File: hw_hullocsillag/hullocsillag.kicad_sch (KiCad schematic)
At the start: 38 parts, among them J1 Conn_2Rows-05Pins, Q1 AO3401A, Q2 AO3401A, Q3 AO3401A, SW2 SW_DPST_x2, T1 Tab, T2 Tab, T3 Tab, U1 PY32F002AF15P6TU

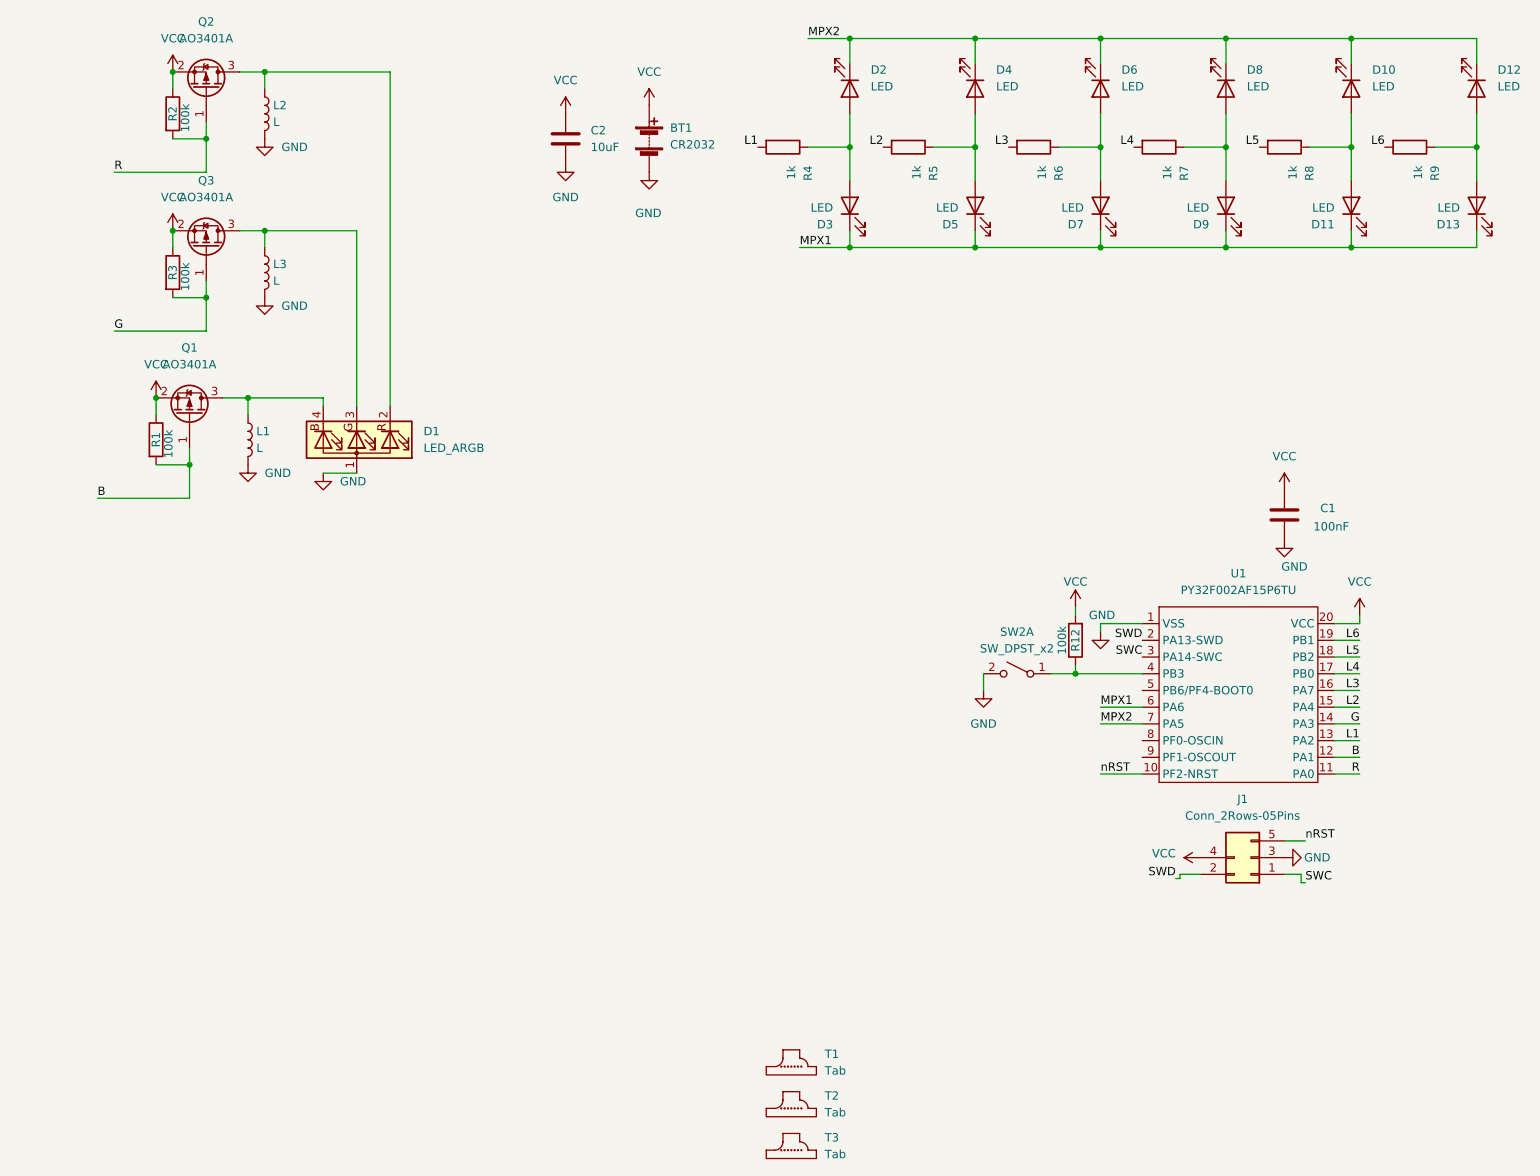
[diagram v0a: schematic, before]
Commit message: Hullocsillag updated, new led driver
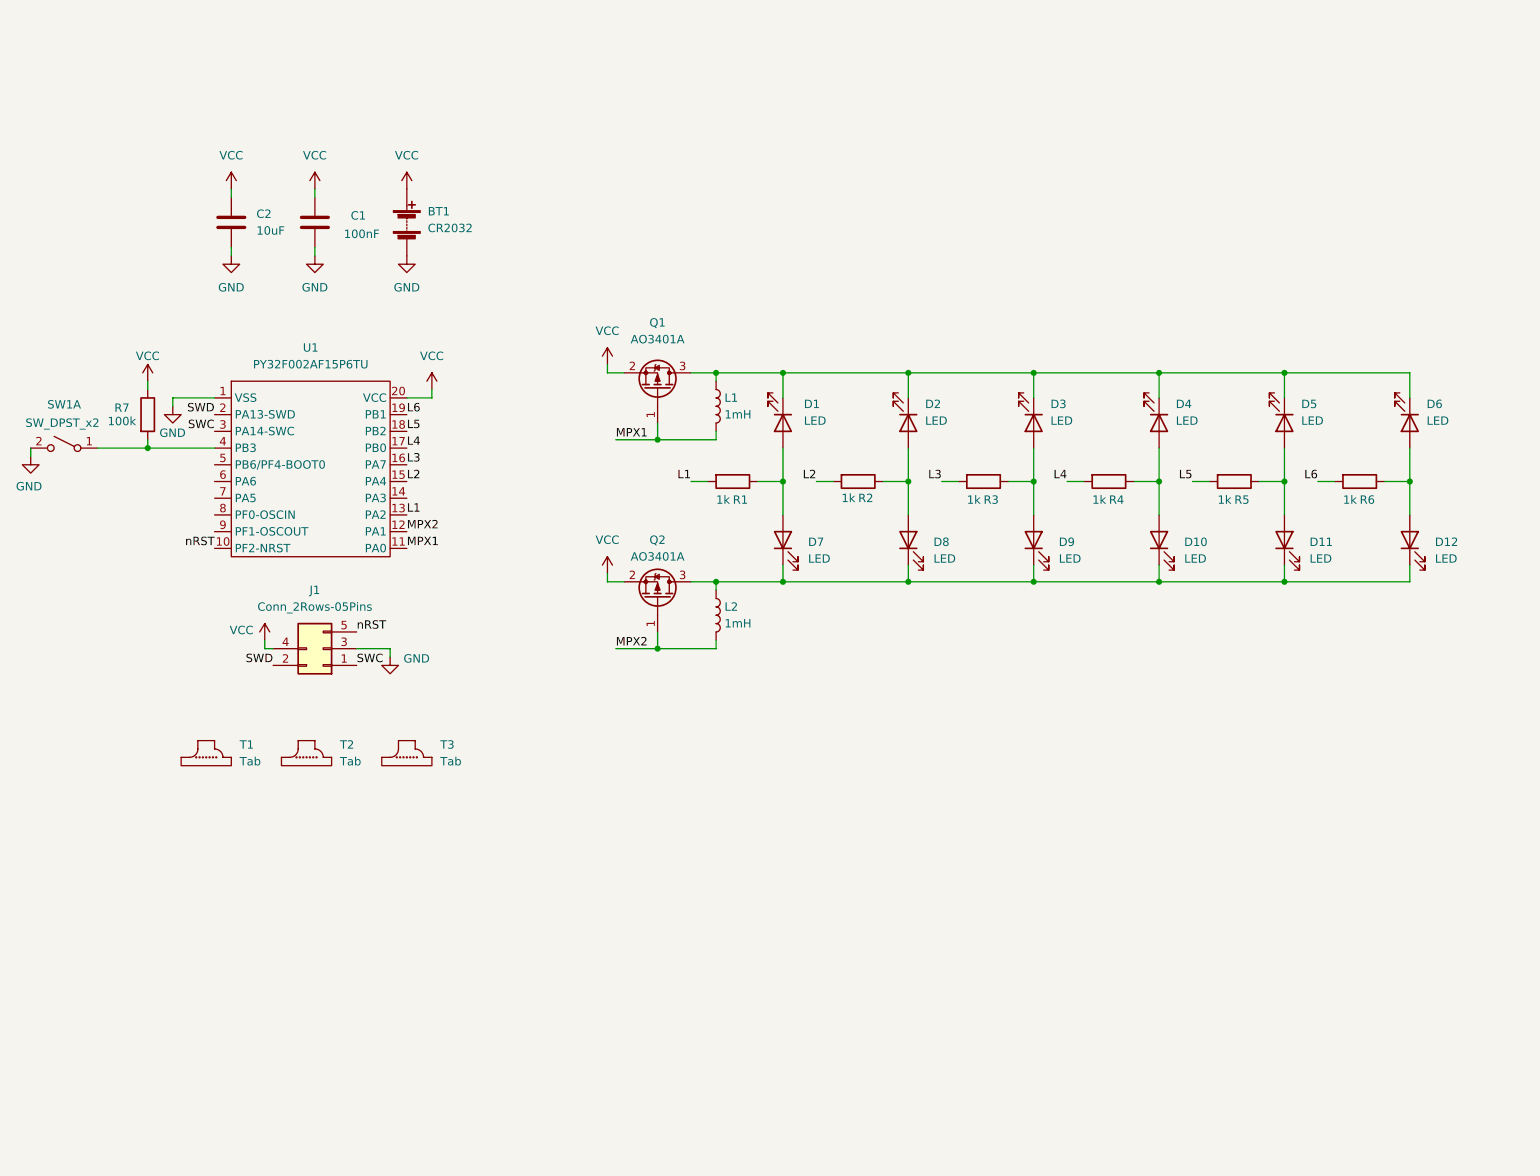
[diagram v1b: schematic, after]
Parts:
- removed D1: LED_ARGB, hullocsillag:LED_RGB_Wuerth-PLCC4_3.2x2.8mm_150141M173100, symbol Device:LED_ARGB
- removed L3: L, Inductor_SMD:L_1008_2520Metric, symbol Device:L
- removed Q3: AO3401A, hullocsillag:SOT-23, symbol Transistor_FET:AO3401A
- removed R1, R12, R2, R3: 100k, Resistor_SMD:R_0603_1608Metric, symbol Device:R
- added R7: 100k, Resistor_SMD:R_0603_1608Metric, symbol Device:R
- L1, L2: value L -> 1mH
- renumbered D2 to D1, D9 to D10, D13 to D12, D4 to D2, D6 to D3, D8 to D4, D10 to D5, D12 to D6, D3 to D7, D5 to D8, D7 to D9, R4 to R1, R5 to R2, R6 to R3, R7 to R4, R8 to R5, R9 to R6, SW2 to SW1
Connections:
- net GND: no longer L1.2, L2.2
- net MPX1: now also L1.2, Q1.1 (G), U1.11 (PA0); no longer D10.1 (K), D11.1 (K), D12.1 (K), D7.1 (K), D8.1 (K), D9.1 (K), U1.6 (PA6)
- net MPX2: now also L2.2, Q2.1 (G), U1.12 (PA1); no longer D1.1 (K), D2.1 (K), D3.1 (K), D4.1 (K), D5.1 (K), D6.1 (K), U1.7 (PA5)
- net VCC: now also R7.1
- net at SW1.1 (A), U1.4 (PB3): now also R7.2
- net at L2.1, Q2.3 (D): now also D10.1 (K), D11.1 (K), D12.1 (K), D7.1 (K), D8.1 (K), D9.1 (K)
- net at L1.1, Q1.3 (D): now also D1.1 (K), D2.1 (K), D3.1 (K), D4.1 (K), D5.1 (K), D6.1 (K)
- removed net B: Q1.1 (G), U1.12 (PA1)
- net G: no longer names the net of U1.14 (PA3)
- removed net R: Q2.1 (G), U1.11 (PA0)
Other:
- moved on the sheet: BT1, C1, C2, D1, D10, D11, D12, D2, D3, D4, D5, D6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

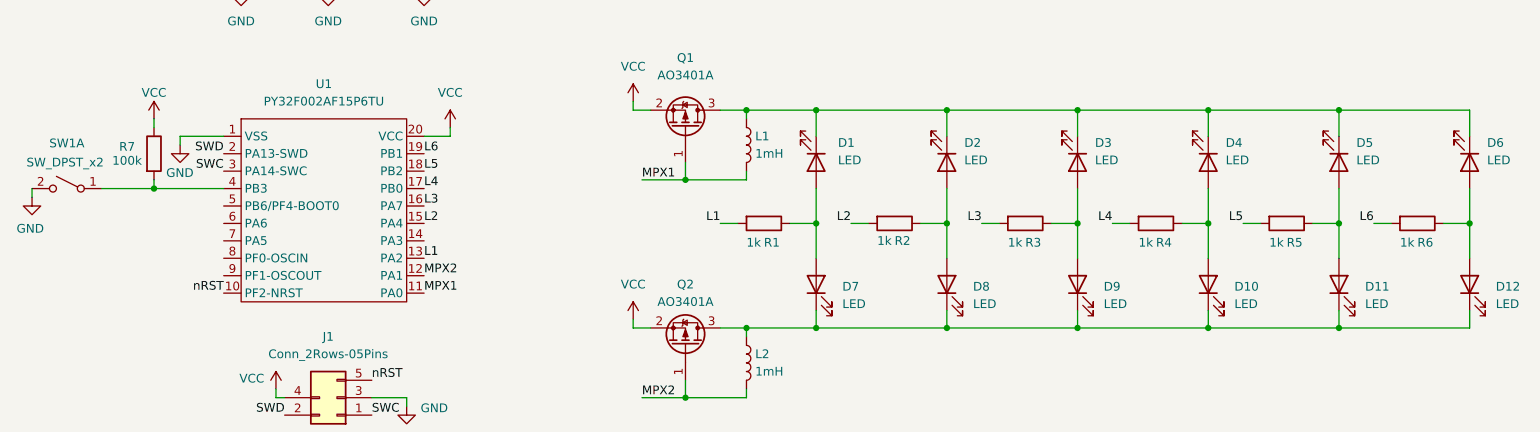
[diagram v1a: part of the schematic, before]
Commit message: Hullocsillag routed, C2 capacitor relocated, silkscreen added.
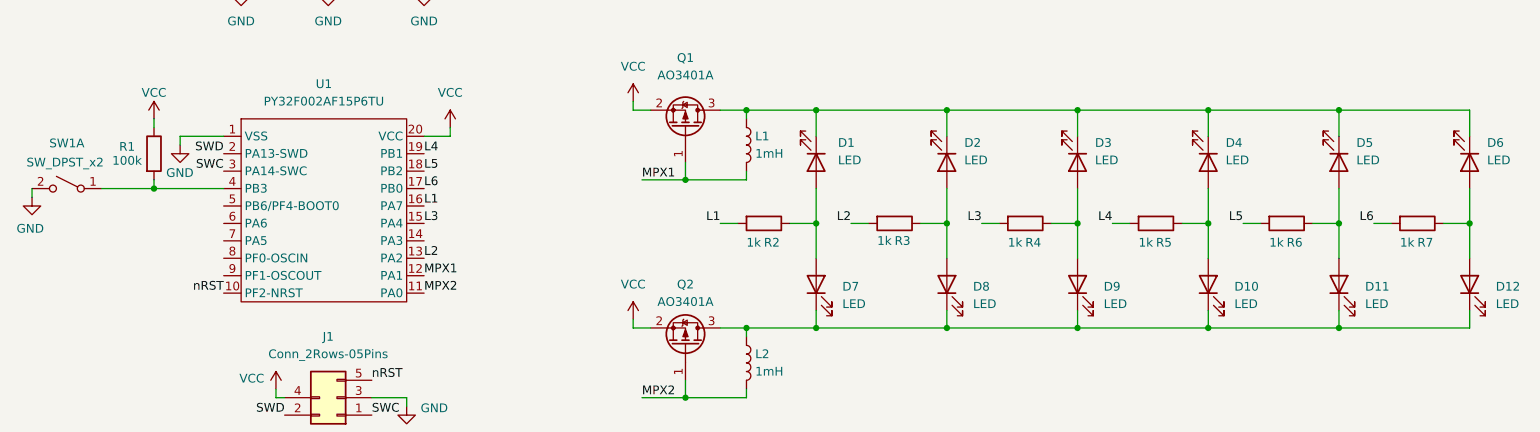
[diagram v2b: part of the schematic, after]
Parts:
- renumbered R7 to R1, R1 to R2, R2 to R3, R3 to R4, R4 to R5, R5 to R6, R6 to R7
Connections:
- net L1: now also U1.16 (PA7); no longer U1.13 (PA2)
- net L2: now also U1.13 (PA2); no longer U1.15 (PA4)
- net L3: now also U1.15 (PA4); no longer U1.16 (PA7)
- net L4: now also U1.19 (PB1); no longer U1.17 (PB0)
- net L6: now also U1.17 (PB0); no longer U1.19 (PB1)
- net MPX1: now also U1.12 (PA1); no longer U1.11 (PA0)
- net MPX2: now also U1.11 (PA0); no longer U1.12 (PA1)
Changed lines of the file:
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@@
 		)
 	)
-	(label "L4"
+	(label "L6"
 		(at 101.6 83.82 0)
 		(effects
@@
 		)
 	)
-	(label "L6"
+	(label "L4"
 		(at 101.6 78.74 0)
 		(effects
@@
 		)
 	)
-	(label "MPX2"
+	(label "MPX1"
 		(at 101.6 96.52 0)
 		(effects
@@
 		)
 	)
-	(label "L3"
+	(label "L1"
 		(at 101.6 86.36 0)
 		(effects
@@
 		)
 	)
-	(label "MPX1"
+	(label "MPX2"
 		(at 101.6 99.06 0)
 		(effects
@@
 		)
 	)
-	(label "L1"
+	(label "L2"
 		(at 101.6 93.98 0)
 		(effects
@@
 		)
 	)
-	(label "L2"
+	(label "L3"
 		(at 101.6 88.9 0)
 		(effects
@@
 		(on_board yes)
 		(dnp no)
-		(property "Reference" "R6"
+		(property "Reference" "R7"
 			(at 246.38 91.694 90)
 			(effects
@@
 			(project ""
 				(path "/30f28fd8-ef05-4208-b612-7ffefcdba2ba"
-					(reference "R6")
+					(reference "R7")
 					(unit 1)
 				)
@@
 		(on_board yes)
 		(dnp no)
-		(property "Reference" "R4"
+		(property "Reference" "R5"
 			(at 208.28 91.694 90)
 			(effects
@@
 			(project ""
 				(path "/30f28fd8-ef05-4208-b612-7ffefcdba2ba"
-					(reference "R4")
+					(reference "R5")
 					(unit 1)
 				)
@@
 		(on_board yes)
 		(dnp no)
-		(property "Reference" "R3"
+		(property "Reference" "R4"
 			(at 189.23 91.694 90)
 			(effects
@@
 			(project ""
 				(path "/30f28fd8-ef05-4208-b612-7ffefcdba2ba"
-					(reference "R3")
+					(reference "R4")
 					(unit 1)
 				)
@@
 		(on_board yes)
 		(dnp no)
-		(property "Reference" "R1"
+		(property "Reference" "R2"
 			(at 151.13 91.694 90)
 			(effects
@@
 			(project ""
 				(path "/30f28fd8-ef05-4208-b612-7ffefcdba2ba"
-					(reference "R1")
+					(reference "R2")
 					(unit 1)
 				)
@@
 		(on_board yes)
 		(dnp no)
-		(property "Reference" "R2"
+		(property "Reference" "R3"
 			(at 170.18 91.44 90)
 			(effects
@@
 			(project ""
 				(path "/30f28fd8-ef05-4208-b612-7ffefcdba2ba"
-					(reference "R2")
+					(reference "R3")
 					(unit 1)
 				)
@@
 		(on_board yes)
 		(dnp no)
-		(property "Reference" "R5"
+		(property "Reference" "R6"
 			(at 227.33 91.694 90)
 			(effects
@@
 			(project ""
 				(path "/30f28fd8-ef05-4208-b612-7ffefcdba2ba"
-					(reference "R5")
+					(reference "R6")
 					(unit 1)
 				)
@@
 		(on_board yes)
 		(dnp no)
-		(property "Reference" "R7"
+		(property "Reference" "R1"
 			(at 57.15 77.724 0)
 			(effects
@@
 			(project "hullocsillag"
 				(path "/30f28fd8-ef05-4208-b612-7ffefcdba2ba"
-					(reference "R7")
-					(unit 1)
-				)
+					(reference "R1")
+					(unit 1)
+				)

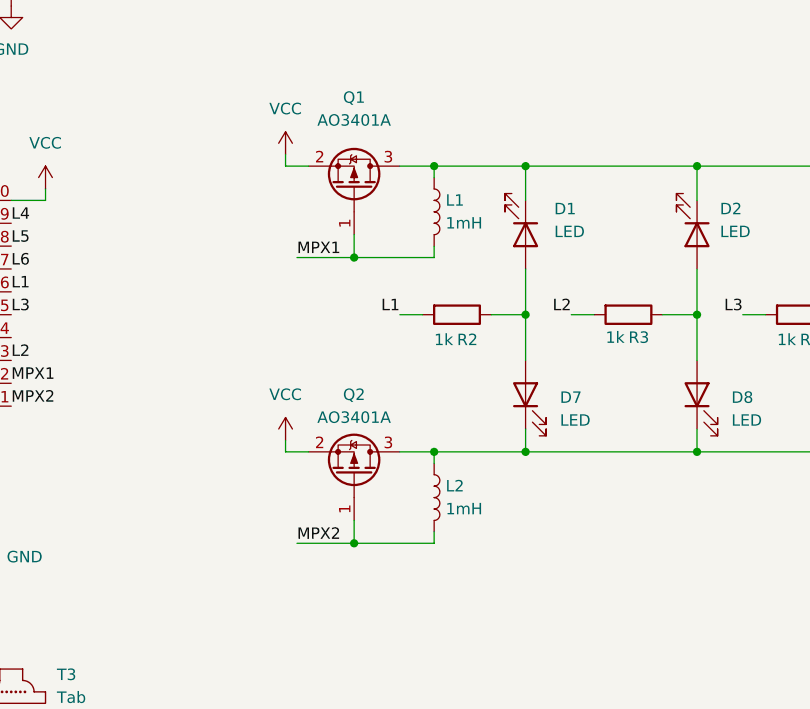
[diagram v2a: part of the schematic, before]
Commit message: Inductor updated, pull-up resistor added, filling reworked
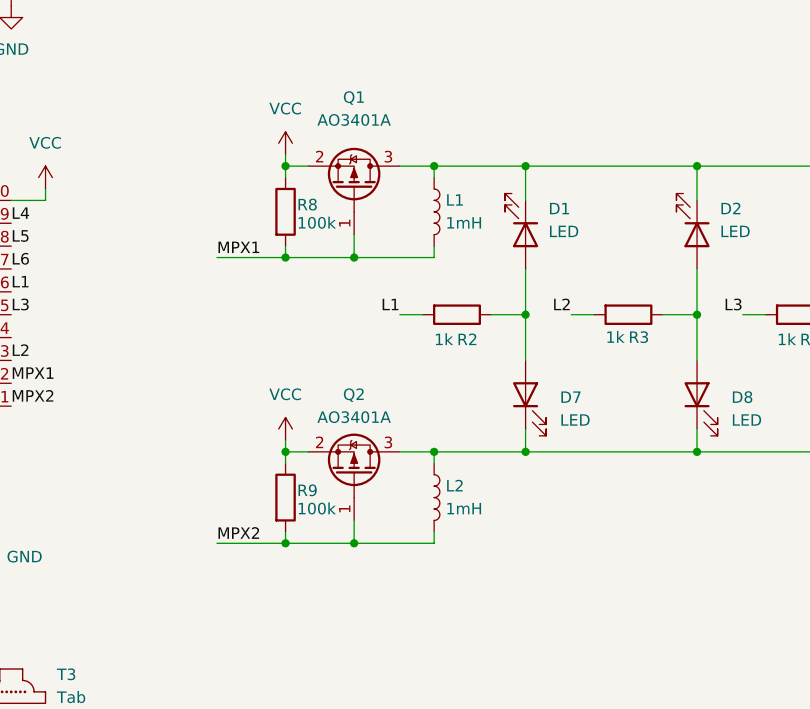
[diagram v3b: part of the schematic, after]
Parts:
- added R8, R9: 100k, Resistor_SMD:R_0603_1608Metric, symbol Device:R
- L1, L2: footprint Inductor_SMD:L_1008_2520Metric -> Inductor_SMD:L_Ferrocore_DLG-0403
- T1, T2, T3: footprint kikit:Tab -> PCM_kikit:Tab
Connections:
- net MPX1: now also R8.2
- net MPX2: now also R9.2
- net VCC: now also R8.1, R9.1

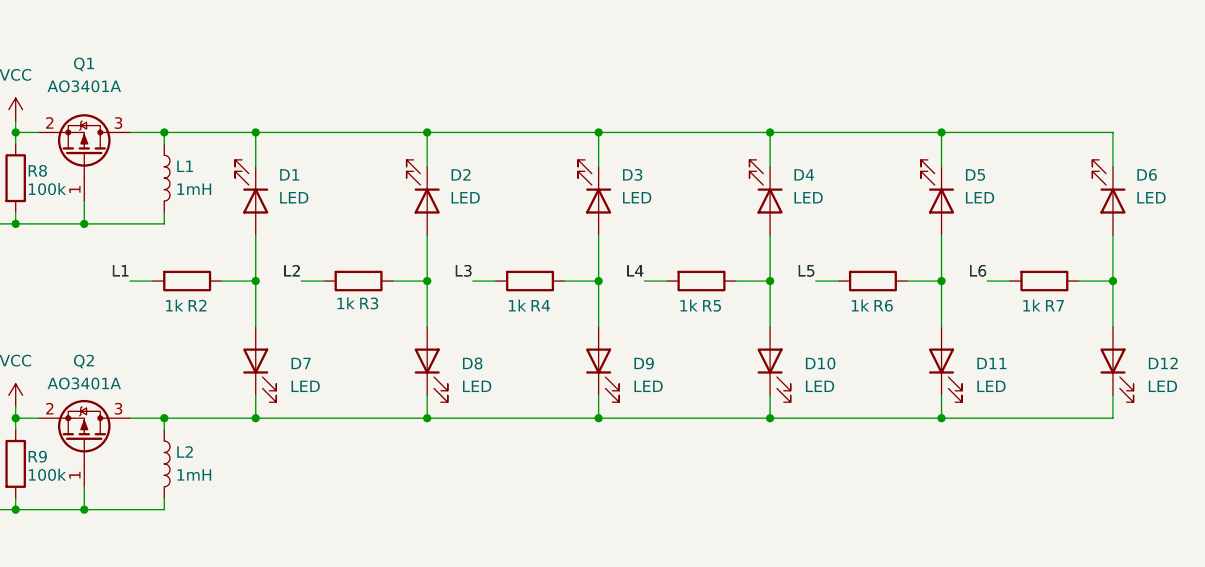
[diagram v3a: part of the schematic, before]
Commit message: Fixed LED resistors.
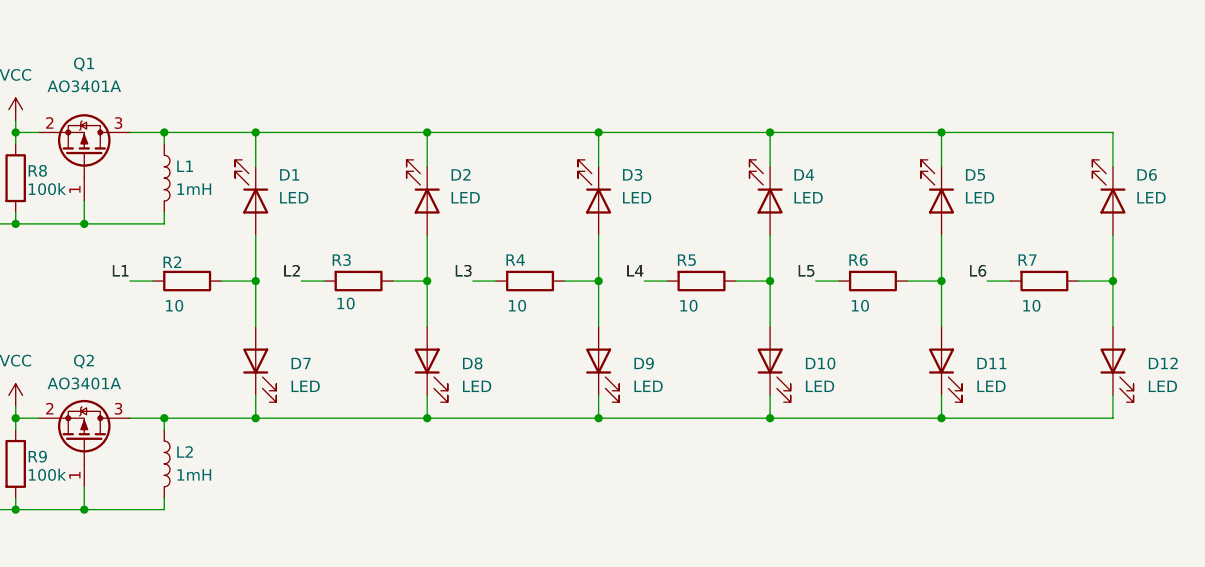
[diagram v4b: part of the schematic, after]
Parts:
- R2, R3, R4, R5, R6, R7: value 1k -> 10
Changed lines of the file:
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@@
 		(dnp no)
 		(property "Reference" "R7"
-			(at 246.38 91.694 90)
-			(effects
-				(font
-					(size 1.27 1.27)
-				)
-				(justify left)
-			)
-		)
-		(property "Value" "1k"
+			(at 243.332 86.614 90)
+			(effects
+				(font
+					(size 1.27 1.27)
+				)
+				(justify left)
+			)
+		)
+		(property "Value" "10"
 			(at 243.84 91.694 90)
 			(effects
@@
 		(dnp no)
 		(property "Reference" "R4"
-			(at 189.23 91.694 90)
-			(effects
-				(font
-					(size 1.27 1.27)
-				)
-				(justify left)
-			)
-		)
-		(property "Value" "1k"
+			(at 186.436 86.614 90)
+			(effects
+				(font
+					(size 1.27 1.27)
+				)
+				(justify left)
+			)
+		)
+		(property "Value" "10"
 			(at 186.69 91.694 90)
 			(effects
@@
 		(dnp no)
 		(property "Reference" "R2"
-			(at 151.13 91.694 90)
-			(effects
-				(font
-					(size 1.27 1.27)
-				)
-				(justify left)
-			)
-		)
-		(property "Value" "1k"
+			(at 148.336 86.868 90)
+			(effects
+				(font
+					(size 1.27 1.27)
+				)
+				(justify left)
+			)
+		)
+		(property "Value" "10"
 			(at 148.59 91.694 90)
 			(effects
@@
 		(dnp no)
 		(property "Reference" "R3"
-			(at 170.18 91.44 90)
-			(effects
-				(font
-					(size 1.27 1.27)
-				)
-				(justify left)
-			)
-		)
-		(property "Value" "1k"
+			(at 167.132 86.614 90)
+			(effects
+				(font
+					(size 1.27 1.27)
+				)
+				(justify left)
+			)
+		)
+		(property "Value" "10"
 			(at 167.64 91.44 90)
 			(effects
@@
 		(dnp no)
 		(property "Reference" "R6"
-			(at 227.33 91.694 90)
-			(effects
-				(font
-					(size 1.27 1.27)
-				)
-				(justify left)
-			)
-		)
-		(property "Value" "1k"
+			(at 224.536 86.614 90)
+			(effects
+				(font
+					(size 1.27 1.27)
+				)
+				(justify left)
+			)
+		)
+		(property "Value" "10"
 			(at 224.79 91.694 90)
 			(effects
@@
 		(dnp no)
 		(property "Reference" "R5"
-			(at 208.28 91.694 90)
-			(effects
-				(font
-					(size 1.27 1.27)
-				)
-				(justify left)
-			)
-		)
-		(property "Value" "1k"
+			(at 205.486 86.614 90)
+			(effects
+				(font
+					(size 1.27 1.27)
+				)
+				(justify left)
+			)
+		)
+		(property "Value" "10"
 			(at 205.74 91.694 90)
 			(effects
